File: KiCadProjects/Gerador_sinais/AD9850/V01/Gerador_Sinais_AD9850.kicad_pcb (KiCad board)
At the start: 2 copper layers, 90 x 100 mm, 3 parts, among them J1 alimentacao analogica, J2 sinais analogicos, J3 comunicacao / sinais digitais

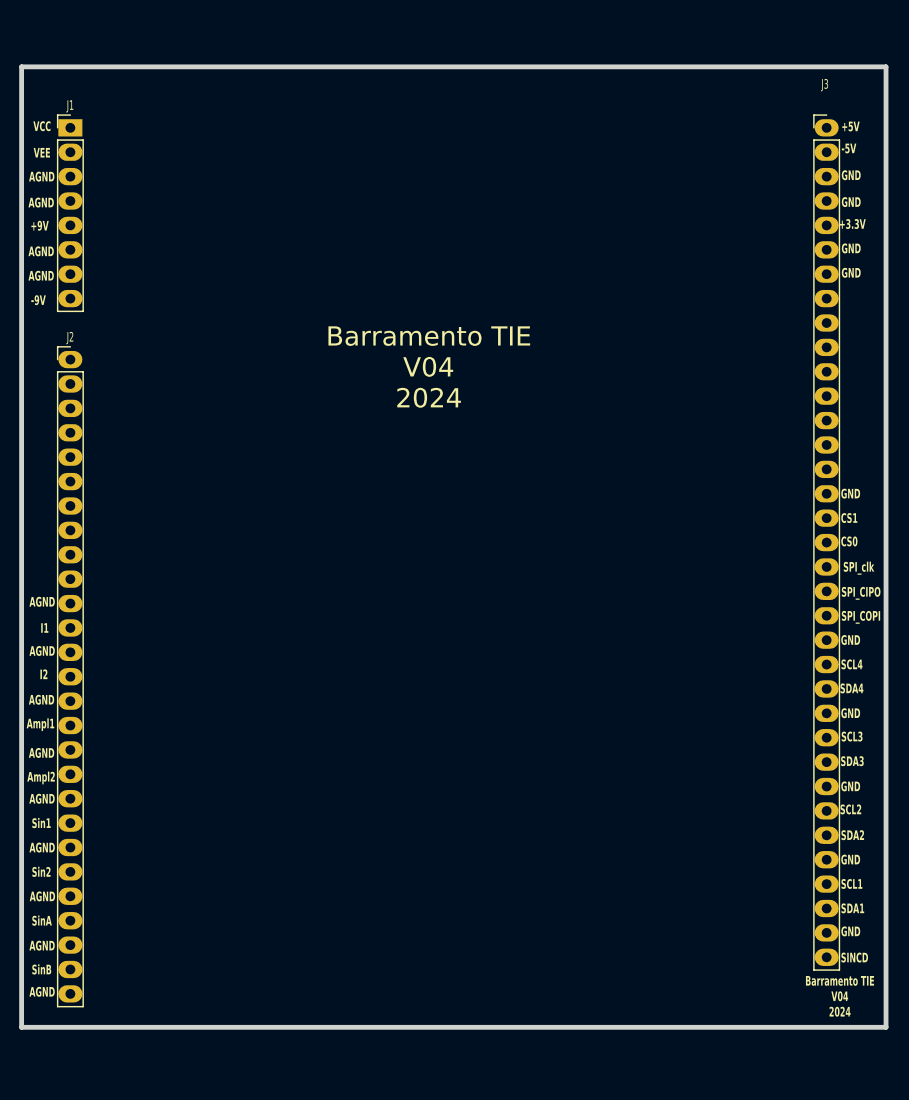
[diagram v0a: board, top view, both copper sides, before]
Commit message: mudanca sinais de entrada e largura trilha
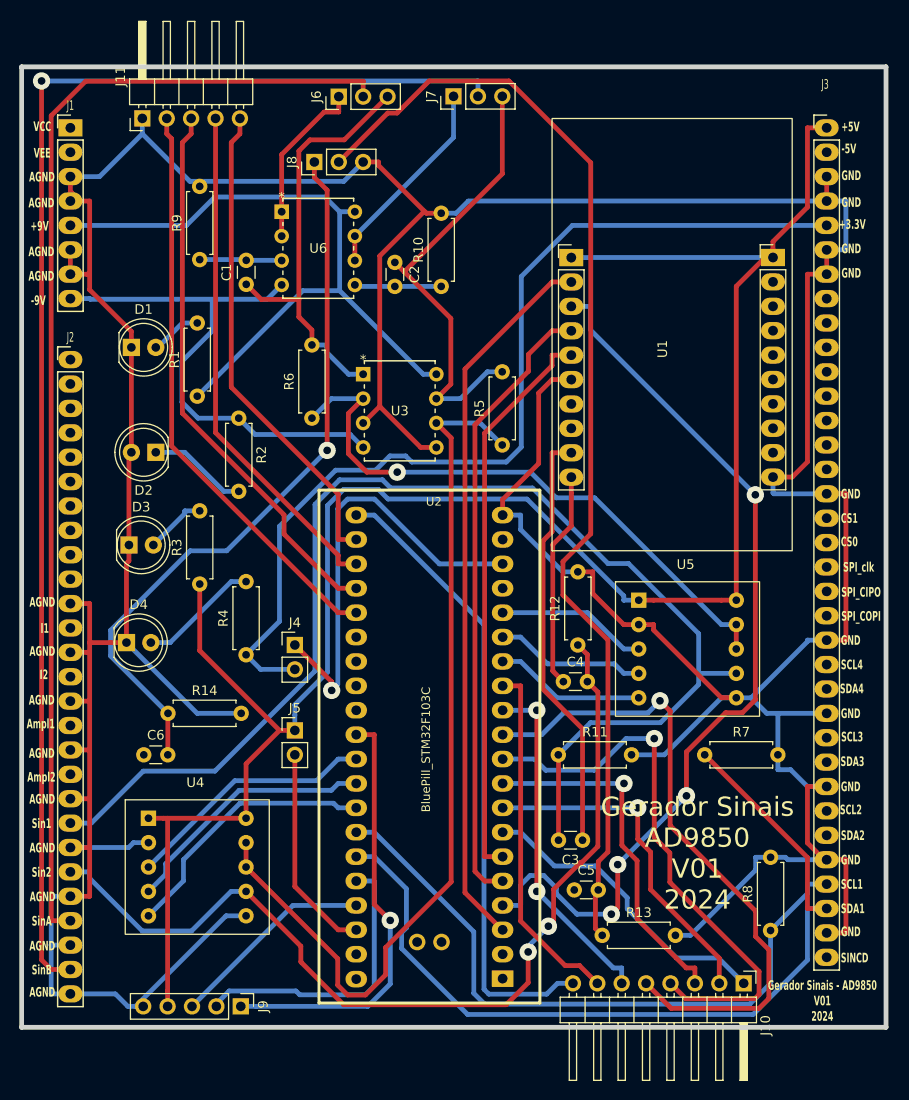
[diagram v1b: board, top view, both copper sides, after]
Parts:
- added C1: 100nF, Capacitor_THT:C_Disc_D3.0mm_W1.6mm_P2.50mm, F.Cu at (125.0, 73.4)
- added C2: 100nF, Capacitor_THT:C_Disc_D3.0mm_W1.6mm_P2.50mm, F.Cu at (140.5, 71.2)
- added C3: 100nF, Capacitor_THT:C_Disc_D3.0mm_W1.6mm_P2.50mm, F.Cu at (160.0, 131.3)
- added C4: 100nF, Capacitor_THT:C_Disc_D3.0mm_W1.6mm_P2.50mm, F.Cu at (158.0, 114.8)
- added C5: 100nF, Capacitor_THT:C_Disc_D3.0mm_W1.6mm_P2.50mm, F.Cu at (159.1, 136.5)
- added C6: 100nF, Capacitor_THT:C_Disc_D3.0mm_W1.6mm_P2.50mm, F.Cu at (114.3, 122.4)
- added D1: LED Blue, LED_THT:LED_D5.0mm, F.Cu at (113.0, 80.0)
- added D2: LED Red, LED_THT:LED_D5.0mm, F.Cu at (115.6, 90.9)
- added D3: LED Green, LED_THT:LED_D5.0mm, F.Cu at (112.8, 100.6)
- added D4: LED - Yelow, LED_THT:LED_D5.0mm, F.Cu at (112.5, 110.7)
- added J10: teclado matricial, Connector_PinHeader_2.54mm:PinHeader_1x08_P2.54mm_Horizontal, F.Cu at (176.8, 146.2)
- added J11: botoes_selecao, Connector_PinHeader_2.54mm:PinHeader_1x05_P2.54mm_Horizontal, F.Cu at (114.2, 56.2)
- added J4: 3.3V STM32, Connector_PinHeader_2.54mm:PinHeader_1x02_P2.54mm_Vertical, F.Cu at (130.0, 111.0)
- added J5: 5.0V STM32, Connector_PinHeader_2.54mm:PinHeader_1x02_P2.54mm_Vertical, F.Cu at (130.0, 119.9)
- added J6: Select SinA, Connector_PinHeader_2.54mm:PinHeader_1x03_P2.54mm_Vertical, F.Cu at (134.6, 53.9)
- added J7: Select SinB, Connector_PinHeader_2.54mm:PinHeader_1x03_P2.54mm_Vertical, F.Cu at (146.6, 53.9)
- added J8: Squad_wave, Connector_PinHeader_2.54mm:PinHeader_1x03_P2.54mm_Vertical, F.Cu at (132.1, 60.7)
- added J9: Encoder KY-040, Connector_PinHeader_2.54mm:PinHeader_1x05_P2.54mm_Vertical, F.Cu at (124.4, 148.6)
- added R1: 1.2k, Resistor_THT:R_Axial_DIN0207_L6.3mm_D2.5mm_P7.62mm_Horizontal, F.Cu at (119.9, 85.1)
- added R10: 160k, Resistor_THT:R_Axial_DIN0207_L6.3mm_D2.5mm_P7.62mm_Horizontal, F.Cu at (145.3, 73.7)
- added R11: 160k, Resistor_THT:R_Axial_DIN0207_L6.3mm_D2.5mm_P7.62mm_Horizontal, F.Cu at (157.5, 122.4)
- added R12: 160k, Resistor_THT:R_Axial_DIN0207_L6.3mm_D2.5mm_P7.62mm_Horizontal, F.Cu at (159.5, 111.0)
- added R13: 160k, Resistor_THT:R_Axial_DIN0207_L6.3mm_D2.5mm_P7.62mm_Horizontal, F.Cu at (162.1, 141.2)
- added R14: 160k, Resistor_THT:R_Axial_DIN0207_L6.3mm_D2.5mm_P7.62mm_Horizontal, F.Cu at (116.8, 118.1)
- added R2: 1.2k, Resistor_THT:R_Axial_DIN0207_L6.3mm_D2.5mm_P7.62mm_Horizontal, F.Cu at (124.2, 87.4)
- added R3: 390, Resistor_THT:R_Axial_DIN0207_L6.3mm_D2.5mm_P7.62mm_Horizontal, F.Cu at (120.1, 104.6)
- added R4: 240, Resistor_THT:R_Axial_DIN0207_L6.3mm_D2.5mm_P7.62mm_Horizontal, F.Cu at (125.0, 112.0)
- added R5: 51k, Resistor_THT:R_Axial_DIN0207_L6.3mm_D2.5mm_P7.62mm_Horizontal, F.Cu at (151.6, 90.2)
- added R6: 51k, Resistor_THT:R_Axial_DIN0207_L6.3mm_D2.5mm_P7.62mm_Horizontal, F.Cu at (131.8, 87.4)
- added R7: 4k7, Resistor_THT:R_Axial_DIN0207_L6.3mm_D2.5mm_P7.62mm_Horizontal, F.Cu at (172.7, 122.4)
- added R8: 4k7, Resistor_THT:R_Axial_DIN0207_L6.3mm_D2.5mm_P7.62mm_Horizontal, F.Cu at (179.6, 140.7)
- added R9: 160k, Resistor_THT:R_Axial_DIN0207_L6.3mm_D2.5mm_P7.62mm_Horizontal, F.Cu at (120.1, 70.9)
- added U1: AD9850_module, AD9850_module:AD9850_module, F.Cu at (168.8, 80.2)
- added U2: BluePill_STM32F103C, BluePill_STM32:BluePill_STM32F103C, F.Cu at (151.7, 145.7)
- added U3: AD828AN, AD828:AD828, F.Cu at (137.2, 82.8)
- added U4: X9c10x, X9c10X_module:X9c10X_module, F.Cu at (119.9, 134.1)
- added U5: X9c10x, X9c10X_module:X9c10X_module, F.Cu at (170.9, 111.4)
- added U6: AD828AN, AD828:AD828, F.Cu at (128.7, 65.9)
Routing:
- net Earth: track 0.00 -> 497.0 mm
- net +5V: track 0.00 -> 209.8 mm
- net SinB: track 0.00 -> 142.0 mm, vias 0 -> 1
- net Sin1: track 0.00 -> 132.8 mm
- net SinA: track 0.00 -> 121.4 mm
- net SQ1: track 0.00 -> 117.7 mm
- net +3.3V: track 0.00 -> 101.4 mm
- net Sin2: track 0.00 -> 98.2 mm, vias 0 -> 2
- net Net-(U1-UD): track 0.00 -> 95.5 mm, vias 0 -> 4
- net Net-(U3--IN2): track 0.00 -> 93.8 mm
- net SDA1: track 0.00 -> 90.3 mm
- net SQ2: track 0.00 -> 76.3 mm, vias 0 -> 1
- net Net-(U1-CLK): track 0.00 -> 74.9 mm
- net +9V: track 0.00 -> 72.7 mm
- net SCL1: track 0.00 -> 69.1 mm
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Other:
- board text added: "Gerador Sinais - AD9850 V01 2024"
- board text added: "Gerador Sinais AD9850 V01 2024"
- board text removed: "Barramento TIE V04 2024"

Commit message: todas conexoes feitas
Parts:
- moved C4 32.9 mm to (129.5, 98.3), turned to -90 degrees
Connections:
- R7 pad 2: Earth -> +3.3V
- R8 pad 2: Earth -> +3.3V
- U1 pad 7: unconnected-(U1-SQ_1-Pad7) -> SQ_AD1
- U1 pad 8: unconnected-(U1-SQ_2-Pad8) -> SQ_AD2
- U2 pad 10: M4 -> Ampl2
- U2 pad 28: unconnected-(U2-PA11_USB_D--Pad28) -> M4
- U2 pad 29: unconnected-(U2-PA12_USBD+-Pad29) -> M3
- U2 pad 9: M3 -> Ampl1
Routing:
- net Ampl2: track 0.00 -> 213.0 mm, vias 0 -> 2
- net Sin1: track 132.8 -> 217.9 mm, vias 0 -> 2
- net Sin2: track 98.2 -> 175.7 mm, vias 2 -> 3
- net Ampl1: track 0.00 -> 76.8 mm
- net SQ_AD2: track 0.00 -> 65.9 mm, vias 0 -> 1
- net +3.3V: track 101.4 -> 166.1 mm, vias 0 -> 2
- net Net-(J4-Pin_1): track 45.9 -> 104.6 mm, vias 1 -> 3
- net SQ_AD1: track 0.00 -> 53.3 mm
- net M5: track 67.8 -> 36.5 mm
- net Net-(U1-UD): track 95.5 -> 71.2 mm, vias 4 -> 0
- net M3: track 37.2 -> 60.0 mm, vias 1 -> 0
- net SDA1: track 90.3 -> 111.1 mm, vias 0 -> 2
- net +5V: track 209.8 -> 228.1 mm, vias 0 -> 2
- net SCL1: track 69.1 -> 86.7 mm, vias 0 -> 1
- net SQ1: track 117.7 -> 102.8 mm
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
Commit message: todas conexoes feitas
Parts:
- moved J8 89.9 mm to (110.5, 148.0)
- moved J7 35.5 mm to (117.0, 73.5), turned to 180 degrees
- moved J6 22.9 mm to (113.0, 61.5), turned to 0 degrees
- moved C1 15.9 mm to (133.5, 60.0), turned to 180 degrees
- moved C2 12.6 mm to (151.0, 78.0), turned to 180 degrees
- moved J9 5.24 mm to (129.6, 148.0)
- moved R9 4.46 mm to (124.0, 68.6)
- moved J11 0.81 mm to (113.4, 56.0)
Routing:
- net Ampl1: track 76.8 -> 207.8 mm, vias 0 -> 2
- net Ampl2: track 213.0 -> 102.4 mm, vias 2 -> 1
- net Net-(J4-Pin_1): track 104.6 -> 36.8 mm, vias 3 -> 0
- net Sin2: track 175.7 -> 110.6 mm, vias 3 -> 1
- net SinB: track 132.7 -> 79.2 mm
- net SinA: track 124.9 -> 79.5 mm, vias 1 -> 0
- net SQ2: track 77.8 -> 32.5 mm, vias 1 -> 0
- net +3.3V: track 166.1 -> 208.9 mm, vias 2 -> 1
- net SDA1: track 111.1 -> 76.4 mm, vias 2 -> 1
- net Earth: track 489.3 -> 472.6 mm, vias 1 -> 0
- net Net-(U6-+IN1): track 8.57 -> 25.0 mm
- net SCL1: track 86.7 -> 71.7 mm
- net Net-(U3--IN2): track 96.2 -> 82.4 mm, vias 0 -> 3
- net +5V: track 228.1 -> 218.1 mm, vias 2 -> 1
- net Sin1_filter: track 17.9 -> 27.9 mm
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
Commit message: Baseado barramento v04 - Finalizado
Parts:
- moved J5 2.66 mm to (130.1, 117.2)
- renumbered D4 to L+3.3v1, D3 to L+5v1, D1 to L+9v1, D2 to L-9v1, U1 to U1-AD9850, U3 to U3-ganho1, U4 to U4-DigPot2, U5 to U5-DigPot1, U6 to U6-filtro-saida1
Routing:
- net Earth: track 472.6 -> 123.8 mm
- net En2: track 24.6 -> 26.9 mm
- net Pot2_CS_(X9c104): track 28.0 -> 29.7 mm
- net Net-(J5-Pin_2): track 28.1 -> 26.6 mm
- net +5V: track 218.1 -> 219.6 mm
- net Down_gain: track 65.8 -> 66.9 mm
- net Net-(U1-AD9850-RESET): track 59.0 -> 57.9 mm
- net freq+: track 53.5 -> 52.6 mm
- net Net-(U3-ganho1--IN1): track 61.7 -> 62.4 mm
- net Pot2_X9c10x_U/D: track 27.2 -> 27.9 mm
- net M3: track 60.3 -> 60.9 mm
- net M2: track 34.8 -> 34.2 mm
- added copper zone on B.Cu, net Earth
- added copper zone on F.Cu, net Earth
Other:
- board text added: "Sin1_filter"
- board text added: "Sin1_gain"
- board text added: "Sin2_filter"
- board text added: "Sin2_gain"

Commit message: temp
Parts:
- added U7-bufferAD9850: AD828AN, AD828:AD828, F.Cu at (125.9, 111.8)
- moved R13 64.0 mm to (149.6, 78.5), turned to -90 degrees
- moved C5 63.9 mm to (149.6, 73.3), turned to -90 degrees
- moved C3 62.3 mm to (137.9, 73.0), turned to -90 degrees
- moved C1 61.1 mm to (111.7, 117.1), turned to -90 degrees
- moved C6 57.4 mm to (143.9, 73.2), turned to -90 degrees
- moved R9 55.1 mm to (111.6, 122.3), turned to -90 degrees
- moved R3 51.4 mm to (153.9, 65.9), turned to 180 degrees
- moved R11 48.3 mm to (137.9, 78.3), turned to -90 degrees
- moved R14 48.0 mm to (143.9, 78.5), turned to -90 degrees
- moved L+3.3v1 44.5 mm to (117.5, 66.5)
- moved R12 42.2 mm to (132.8, 78.3), turned to -90 degrees
- moved J6 40.0 mm to (152.5, 55.5), turned to -90 degrees
- moved C2 38.1 mm to (113.0, 80.9), turned to 0 degrees
- moved R4 37.3 mm to (112.1, 77.0)
- moved L+5v1 36.0 mm to (124.2, 66.5)
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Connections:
- C3 pad 2: Sin1 -> Sin1_PA
- C4 pad 2: Sin2 -> Sin2_PA
- R11 pad 1: Sin1 -> Sin1_PA
- R12 pad 1: Sin2 -> Sin2_PA
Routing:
- net Earth: track 123.8 -> 468.0 mm
- net Ampl2: track 102.1 -> 212.9 mm
- net Ampl1: track 207.3 -> 111.8 mm, vias 2 -> 1
- net Sin2: track 110.6 -> 36.3 mm
- net Sin2_PA: track 0.00 -> 69.5 mm, vias 0 -> 1
- net SQ2: track 32.5 -> 90.4 mm
- net SinA: track 79.5 -> 136.5 mm
- net SinB: track 79.2 -> 130.2 mm, vias 0 -> 1
- net Sin1_PA: track 0.00 -> 47.5 mm
- net +3.3V: track 208.5 -> 163.1 mm, vias 1 -> 0
- net Sin2_gain: track 49.7 -> 94.5 mm, vias 0 -> 1
- net SQ_AD2: track 67.0 -> 22.2 mm
- net SQ_AD1: track 53.9 -> 17.6 mm
- net Sin1_filter: track 27.9 -> 63.8 mm, vias 0 -> 1
- net Up_gain: track 59.8 -> 91.7 mm, vias 0 -> 3
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
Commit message: temp
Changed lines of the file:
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@@
     (property "ki_keywords" "R res resistor")
     (attr through_hole)
-    (fp_text reference "R1" (at 7.59 2.212) (layer "F.SilkS")
+    (fp_text reference "R1" (at 4.51 -2.8) (layer "F.SilkS")
         (effects (font (size 1 1) (thickness 0.15)))
     )
@@
     (property "ki_keywords" "cap capacitor")
     (attr through_hole)
-    (fp_text reference "C2" (at 1.25 2.2) (layer "F.SilkS")
+    (fp_text reference "C2" (at 1.45 -2.1) (layer "F.SilkS")
         (effects (font (size 1 1) (thickness 0.15)))
     )
@@
     (property "ki_keywords" "connector")
     (attr through_hole)
-    (fp_text reference "J5" (at 0.1 4.775) (layer "F.SilkS")
+    (fp_text reference "J5" (at 0.4 -2.125) (layer "F.SilkS")
         (effects (font (size 1 1) (thickness 0.15)))
     )
-    (fp_text value "5.0V STM32" (at -2.31 1.515 90) (layer "F.SilkS")
+    (fp_text value "5.0V STM32" (at -2.31 1.175 90) (layer "F.SilkS")
         (effects (font (size 1 0.6) (thickness 0.15)))
     )
@@
     (property "ki_keywords" "R res resistor")
     (attr through_hole)
-    (fp_text reference "R13" (at 1.568 2.256 90) (layer "F.SilkS")
+    (fp_text reference "R13" (at 3.72 2.1 90) (layer "F.SilkS")
         (effects (font (size 1 1) (thickness 0.15)))
     )
@@
     (property "ki_keywords" "LED diode")
     (attr through_hole)
-    (fp_text reference "L+3.3v1" (at 1.27 -3.96) (layer "F.SilkS")
+    (fp_text reference "L+3.3v1" (at 1.125 3.9) (layer "F.SilkS")
         (effects (font (size 1 1) (thickness 0.15)))
     )
@@
     (property "ki_keywords" "R res resistor")
     (attr through_hole)
-    (fp_text reference "R7" (at 3.81 -2.37) (layer "F.SilkS")
+    (fp_text reference "R7" (at -0.19 2.2) (layer "F.SilkS")
         (effects (font (size 1 1) (thickness 0.15)))
     )
@@
     (property "Sheetname" "")
     (attr through_hole)
-    (fp_text reference "U5-DigPot1" (at -0.2 -8.8) (layer "F.SilkS")
+    (fp_text reference "U5-DigPot1" (at 8.37 -0.21 -90) (layer "F.SilkS")
         (effects (font (size 1 1) (thickness 0.15)))
     )
@@
     (property "ki_keywords" "AD828AN")
     (attr through_hole)
-    (fp_text reference "U7-bufferAD9850" (at 3.81 10.26 -90 unlocked) (layer "F.SilkS")
+    (fp_text reference "U7-bufferAD9850" (at 9.61 3.41 unlocked) (layer "F.SilkS")
         (effects (font (size 1 1) (thickness 0.15)))
     )
@@
     (property "ki_keywords" "LED diode")
     (attr through_hole)
-    (fp_text reference "L+5v1" (at 1.27 -3.96) (layer "F.SilkS")
+    (fp_text reference "L+5v1" (at 1.59 3.8) (layer "F.SilkS")
         (effects (font (size 1 1) (thickness 0.15)))
     )
@@
     (property "ki_keywords" "R res resistor")
     (attr through_hole)
-    (fp_text reference "R2" (at 3.81 -2.37) (layer "F.SilkS")
+    (fp_text reference "R2" (at -1.89 1.4) (layer "F.SilkS")
         (effects (font (size 1 1) (thickness 0.15)))
     )
@@
     (property "ki_keywords" "R res resistor")
     (attr through_hole)
-    (fp_text reference "R3" (at 5.648 2.458) (layer "F.SilkS")
+    (fp_text reference "R3" (at 3.51 -2.3) (layer "F.SilkS")
         (effects (font (size 1 1) (thickness 0.15)))
     )
@@
     (property "ki_keywords" "connector")
     (attr through_hole)
-    (fp_text reference "J11" (at 4.385 -2.27 90) (layer "F.SilkS")
+    (fp_text reference "J11" (at 3.1 -2.38 90) (layer "F.SilkS")
         (effects (font (size 1 1) (thickness 0.15)))
     )
@@
     (property "ki_keywords" "R res resistor")
     (attr through_hole)
-    (fp_text reference "R6" (at 7.81 2.5 90) (layer "F.SilkS")
+    (fp_text reference "R6" (at 3.82 2.2 90) (layer "F.SilkS")
         (effects (font (size 1 1) (thickness 0.15)))
     )
@@
     (property "ki_keywords" "AD828AN")
     (attr through_hole)
-    (fp_text reference "U6-filtro-saida1" (at 3.624 -2.69 90 unlocked) (layer "F.SilkS")
+    (fp_text reference "U6-filtro-saida1" (at -1.8 3.6 unlocked) (layer "F.SilkS")
         (effects (font (size 1 1) (thickness 0.15)))
     )
@@
         (effects (font (size 1 1) (thickness 0.15)))
     )
-    (fp_text value "teclado matricial" (at -2.39 2.21 -180) (layer "F.SilkS")
+    (fp_text value "teclado matricial" (at -2.62 8.28 -180) (layer "F.SilkS")
         (effects (font (size 1 0.6) (thickness 0.15)))
     )
@@
     (property "ki_keywords" "AD828AN")
     (attr through_hole)
-    (fp_text reference "U3-ganho1" (at 5.04 -2.404 90 unlocked) (layer "F.SilkS")
+    (fp_text reference "U3-ganho1" (at -1.88 3.9 unlocked) (layer "F.SilkS")
         (effects (font (size 1 1) (thickness 0.15)))
     )
@@
     (property "Sheetname" "")
     (attr through_hole)
-    (fp_text reference "U4-DigPot2" (at -0.2 8.1 90) (layer "F.SilkS")
+    (fp_text reference "U4-DigPot2" (at 8.6 2.6 -180) (layer "F.SilkS")
         (effects (font (size 1 1) (thickness 0.15)))
     )
@@
     (property "ki_keywords" "cap capacitor")
     (attr through_hole)
-    (fp_text reference "C1" (at 1.25 -2.05 90) (layer "F.SilkS")
+    (fp_text reference "C1" (at 1.22 1.9 90) (layer "F.SilkS")
         (effects (font (size 1 1) (thickness 0.15)))
     )
